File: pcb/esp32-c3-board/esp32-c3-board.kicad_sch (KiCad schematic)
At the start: 31 parts, among them P101 CAN, P102 RS485, P3 CONN_1, P4 CONN_1, P5 CONN_1, P6 CONN_1, U1 ESP32-C3-Waveshare, U102 TJA1050, U2 esp32-c3-ebay, U4 6N137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

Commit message: Working version on esp32C3 firmware
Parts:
- R3: value 4K7 -> 2K2
- R4: value 3K3 -> 1K
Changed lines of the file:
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@@
       (effects (font (size 1.016 1.016)))
     )
-    (property "Value" "3K3" (at 162.8648 143.51 90)
+    (property "Value" "1K" (at 162.8648 143.51 90)
       (effects (font (size 1.016 1.016)))
     )
@@
       (effects (font (size 1.016 1.016)))
     )
-    (property "Value" "4K7" (at 187.9854 122.0978 90)
+    (property "Value" "2K2" (at 187.9854 122.0978 90)
       (effects (font (size 1.016 1.016)))
     )

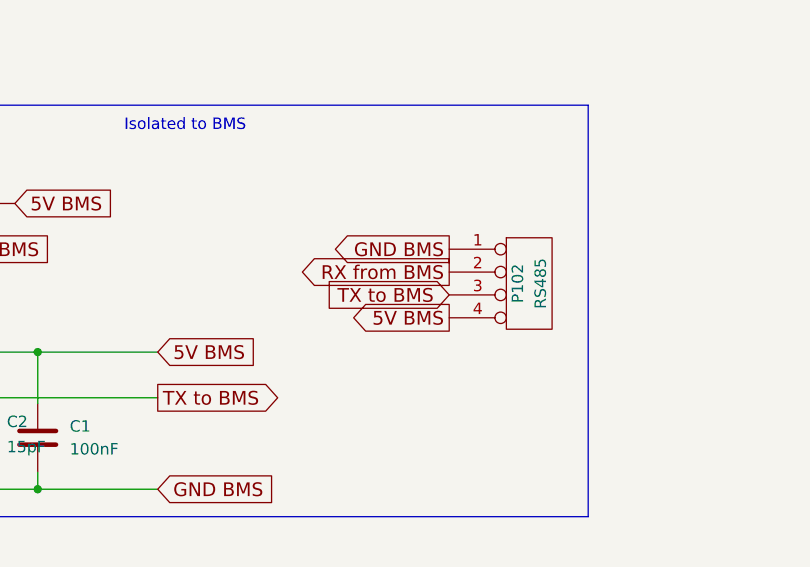
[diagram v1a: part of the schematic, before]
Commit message: messed up bms uart connector
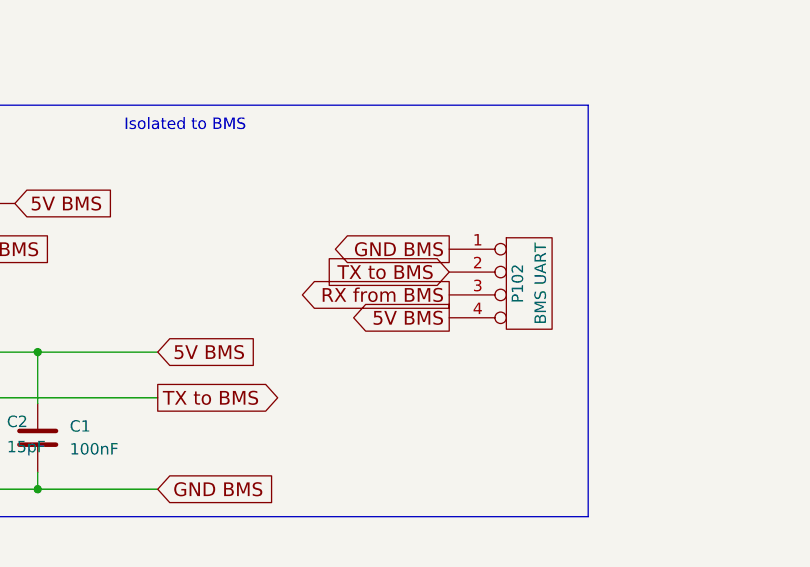
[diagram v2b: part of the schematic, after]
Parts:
- P102: value RS485 -> BMS UART
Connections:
- net RX from BMS: now also P102.3 (P3); no longer P102.2 (P2)
- net TX to BMS: now also P102.2 (P2); no longer P102.3 (P3)

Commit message: Working version connected to real BMS
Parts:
- removed C1, C4: 100nF, Capacitor_SMD:C_0805_2012Metric_Pad1.18x1.45mm_HandSolder, symbol Device:C
- removed C2, C3: 15pF, Capacitor_SMD:C_0805_2012Metric_Pad1.18x1.45mm_HandSolder, symbol Device:C
- removed R3: 2K2, Resistor_SMD:R_0805_2012Metric_Pad1.20x1.40mm_HandSolder, symbol device:R
- removed R4: 1K, Resistor_SMD:R_0805_2012Metric_Pad1.20x1.40mm_HandSolder, symbol device:R
- removed U4, U6: 6N137, Package_DIP:DIP-8_W7.62mm, symbol Isolator:6N137
- added C206 (x2): 10uF, Capacitor_SMD:C_0805_2012Metric_Pad1.18x1.45mm_HandSolder, symbol device:C
- added C206: 10nF, Capacitor_SMD:C_0805_2012Metric_Pad1.18x1.45mm_HandSolder, symbol device:C
- added P1: HW-613, symbol conn:CONN_4
- added R3 (x2): 10K, Resistor_SMD:R_0805_2012Metric_Pad1.20x1.40mm_HandSolder, symbol device:R
- added R3: 3K3, Resistor_SMD:R_0805_2012Metric_Pad1.20x1.40mm_HandSolder, symbol device:R
- added U3: LP2985-3.3, Package_TO_SOT_SMD:SOT-23-5, symbol Regulator_Linear:LP2985-3.3
- added U4: PC817, Package_DIP:DIP-4_W7.62mm, symbol Isolator:PC817
- added U7: STIS0621, Package_SO:SOIC-8_3.9x4.9mm_P1.27mm, symbol Isolator:ADuM1201BR
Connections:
- net 3v3: now also U7.1 (VDD1)
- net 5.8V: now also P1.4 (P4)
- net 5V: now also R3.2
- net BMS-RX: now also U7.2 (VOA)
- net BMS-TX: now also U7.3 (VIB)
- net GND: now also P1.3 (P3), U4.2, U7.4 (GND1)
- net GND BMS: now also C206.2, C206.2, C206.2, R3.2, U3.2 (GND), U7.5 (GND2)
- net RX from BMS: now also U7.7 (VIA)
- net TX to BMS: now also U7.6 (VOB)
- net 12vFused: now reaches C205.1, D203.2 (K), D204.2 (K), TH201.1, U5.1 (12v)
- net 12vFused: now also P1.2 (P2)
- net 5V BMS renamed 12V BMS
- net 12V BMS: now also C206.1, R3.2, U3.1 (VIN)
- new net: R3.1, U4.4
- new net: R3.1, U4.1
- new net: R3.1, U3.3 (ON/~{OFF}), U4.3
- new net: C206.1, U3.4 (BP)
- new net 3.3V BMS: C206.1, U3.5 (VOUT), U7.8 (VDD2)
- no-connect marks 27 -> 25
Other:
- note added: "On requires 1.6v relative to GND"
- note added: "The BMS will wake up if the RX line sends data. Holding the RX High does not result in the BMS staying awake. 3N137 draws 4ma at rest so it cannot be powered when not in use. Other isolators draw about 2mA, so there is no way of avoiding an enable on"
- moved on the sheet: P102, P3, P4, P5, P6

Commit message: Included simulations
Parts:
- P1: footprint (none) -> Connector_PinHeader_2.54mm:PinHeader_1x04_P2.54mm_Vertical
- R3: value 10K -> 22K
- R3: value 3K3 -> 10K
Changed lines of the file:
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@@
       (effects (font (size 1.27 1.27)) (justify right))
     )
-    (property "Footprint" "" (at 156.21 15.875 0)
+    (property "Footprint" "Connector_PinHeader_2.54mm:PinHeader_1x04_P2.54mm_Vertical" (at 156.21 15.875 0)
       (effects (font (size 1.27 1.27)) hide)
     )
@@
       (effects (font (size 1.016 1.016)))
     )
-    (property "Value" "10K" (at 88.9 119.38 90)
+    (property "Value" "22K" (at 88.9 119.38 90)
       (effects (font (size 1.016 1.016)))
     )
@@
       (effects (font (size 1.016 1.016)))
     )
-    (property "Value" "3K3" (at 92.075 131.445 90)
-      (effects (font (size 1.016 1.016)))
-    )
+    (property "Value" "10K" (at 92.075 131.445 90)
+      (effects (font (size 1.016 1.016)))
+    )

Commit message: Added engine Freeze frame functoinality
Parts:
- added C105: 10uF, Capacitor_SMD:C_0805_2012Metric_Pad1.18x1.45mm_HandSolder, symbol device:C
- P101: footprint Connector_Wire:SolderWire-1.5sqmm_1x04_P6mm_D1.7mm_OD3mm_Relief -> Connector_Wire:SolderWire-1.5sqmm_1x04_P6mm_D1.7mm_OD3mm
- TH201: footprint Resistor_THT:R_Axial_DIN0207_L6.3mm_D2.5mm_P7.62mm_Horizontal -> Resistor_SMD:R_2010_5025Metric_Pad1.40x2.65mm_HandSolder
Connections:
- net 5V: now also C105.2
- net GND: now also C105.1
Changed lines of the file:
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@@
   (junction (at 176.53 29.21) (diameter 0) (color 0 0 0 0)
   )
+  (junction (at 81.915 49.53) (diameter 0) (color 0 0 0 0)
+  )
   (junction (at 142.24 46.99) (diameter 0) (color 0 0 0 0)
   )
@@
   )
   (junction (at 122.555 76.2) (diameter 0) (color 0 0 0 0)
+  )
+  (junction (at 81.915 64.77) (diameter 0) (color 0 0 0 0)
   )
   (junction (at 123.825 92.71) (diameter 0) (color 0 0 0 0)
@@
     (stroke (width 0) (type default))
   )
+  (wire (pts (xy 76.2 53.34) (xy 76.2 49.53))
+    (stroke (width 0) (type default))
+  )
   (wire (pts (xy 145.415 76.2) (xy 153.035 76.2))
     (stroke (width 0) (type default))
@@
     (stroke (width 0) (type default))
   )
+  (wire (pts (xy 76.2 64.77) (xy 81.915 64.77))
+    (stroke (width 0) (type default))
+  )
   (wire (pts (xy 130.81 22.86) (xy 130.81 29.21))
     (stroke (width 0) (type default))
@@
     (stroke (width 0) (type default))
   )
+  (wire (pts (xy 81.915 64.77) (xy 81.915 71.12))
+    (stroke (width 0) (type default))
+  )
   (wire (pts (xy 160.02 24.13) (xy 160.02 24.765))
     (stroke (width 0) (type default))
@@
     (stroke (width 0) (type default))
   )
+  (wire (pts (xy 76.2 49.53) (xy 81.915 49.53))
+    (stroke (width 0) (type default))
+  )
   (wire (pts (xy 85.725 49.53) (xy 89.535 49.53))
     (stroke (width 0) (type default))
@@
     (stroke (width 0) (type default))
   )
-  (wire (pts (xy 81.915 63.5) (xy 81.915 71.12))
+  (wire (pts (xy 81.915 63.5) (xy 81.915 64.77))
     (stroke (width 0) (type default))
   )
@@
   )
   (wire (pts (xy 154.94 24.765) (xy 154.94 26.67))
+    (stroke (width 0) (type default))
+  )
+  (wire (pts (xy 76.2 63.5) (xy 76.2 64.77))
     (stroke (width 0) (type default))
   )
@@
       (effects (font (size 1.27 1.27)))
     )
-    (property "Footprint" "Resistor_THT:R_Axial_DIN0207_L6.3mm_D2.5mm_P7.62mm_Horizontal" (at 110.49 29.21 0)
+    (property "Footprint" "Resistor_SMD:R_2010_5025Metric_Pad1.40x2.65mm_HandSolder" (at 110.49 29.21 0)
       (effects (font (size 1.524 1.524)) hide)
     )
@@
       (effects (font (size 1.27 1.27)))
     )
-    (property "Footprint" "Connector_Wire:SolderWire-1.5sqmm_1x04_P6mm_D1.7mm_OD3mm_Relief" (at 98.425 95.885 0)
+    (property "Footprint" "Connector_Wire:SolderWire-1.5sqmm_1x04_P6mm_D1.7mm_OD3mm" (at 98.425 95.885 0)
       (effects (font (size 1.524 1.524)) hide)
     )
@@
         )
       )
+    )
+  )
+  (symbol (lib_id "device:C") (at 76.2 58.42 180) (unit 1)
+    (in_bom yes) (on_board yes) (dnp no)
+    (property "Reference" "C105" (at 76.2 60.96 0)
+      (effects (font (size 1.016 1.016)) (justify left))
+    )
+    (property "Value" "10uF" (at 76.0476 56.261 0)
+      (effects (font (size 1.016 1.016)) (justify left))
+    )
+    (property "Footprint" "Capacitor_SMD:C_0805_2012Metric_Pad1.18x1.45mm_HandSolder" (at 75.2348 54.61 0)
+      (effects (font (size 0.762 0.762)) hide)
+    )
+    (property "Datasheet" "" (at 76.2 58.42 0)
+      (effects (font (size 1.524 1.524)))
+    )
+    (pin "1")
+    (pin "2")
+    (instances
+      (project "ESP32CanBoard"
+        (path "/17502814-a097-4dea-91a7-aec909c8a89f"
+          (reference "C105") (unit 1)
+        )
+      )
+      (project "esp32-c3-board"
+        (path "/f1c311d1-2fb5-46a9-8cac-10128a8ff086"
+          (reference "C1") (unit 1)
+        )
+      )
